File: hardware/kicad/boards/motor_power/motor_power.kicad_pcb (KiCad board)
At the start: 2 copper layers, 104 x 104 mm, 58 parts, among them J1 PWM fra MCU, J2 MCP PWM, J3 DC Motor, J4 3-fase ind, J5 3-fase ud, J6 V1 ud til load, J7 Screw_Terminal_01x03, Q1 IRF540N, Q2 IRF530, SW1 Switch, U1 MCP601, U2 NE555, U3 ILD74, U4 MCP601, U5 IR2110, U6 LM7805, U7 4N25, U8 IR2110

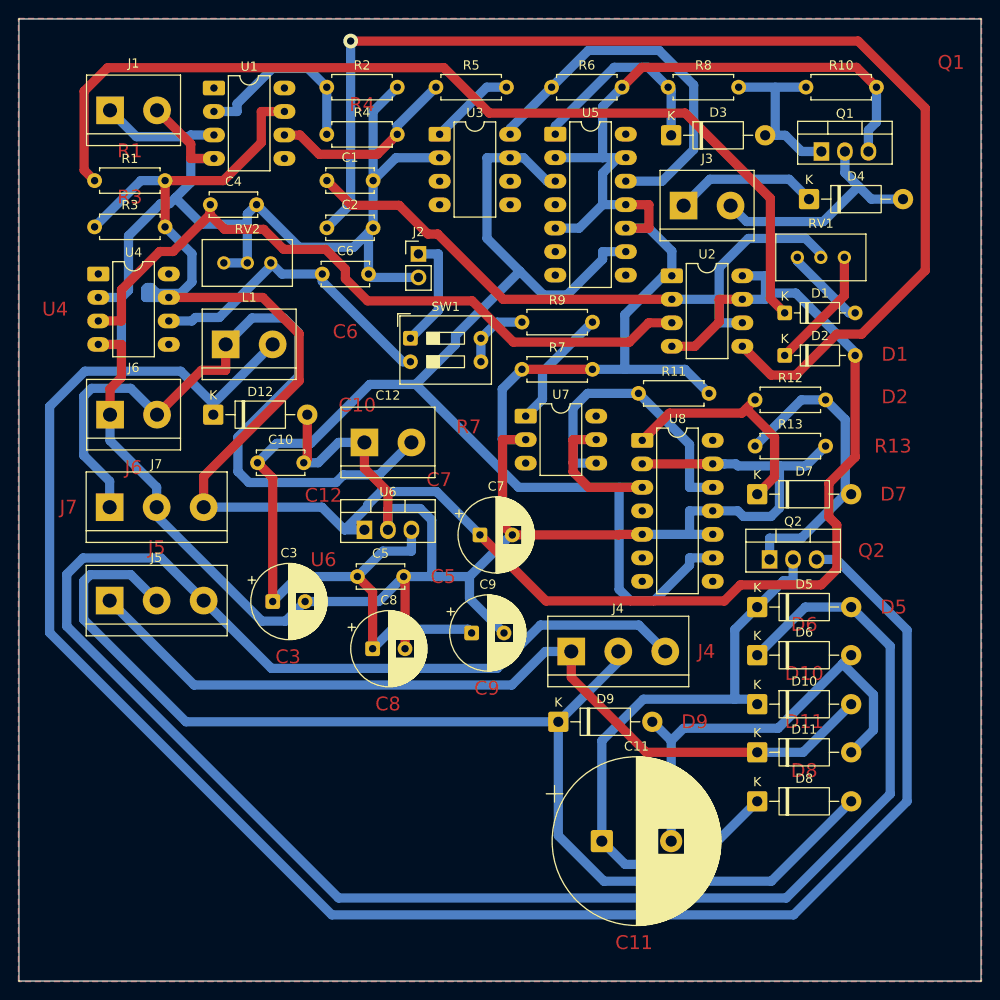
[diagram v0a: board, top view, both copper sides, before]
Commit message: motor_power: re-route with 0 vias (single-sided clean)
Bypass caps placed adjacent to their ICs (C1/C2 by the 555) so the 555-CONT net
no longer needs an inter-layer link. Fully routed: 0 vias, 0 unconnected pads.
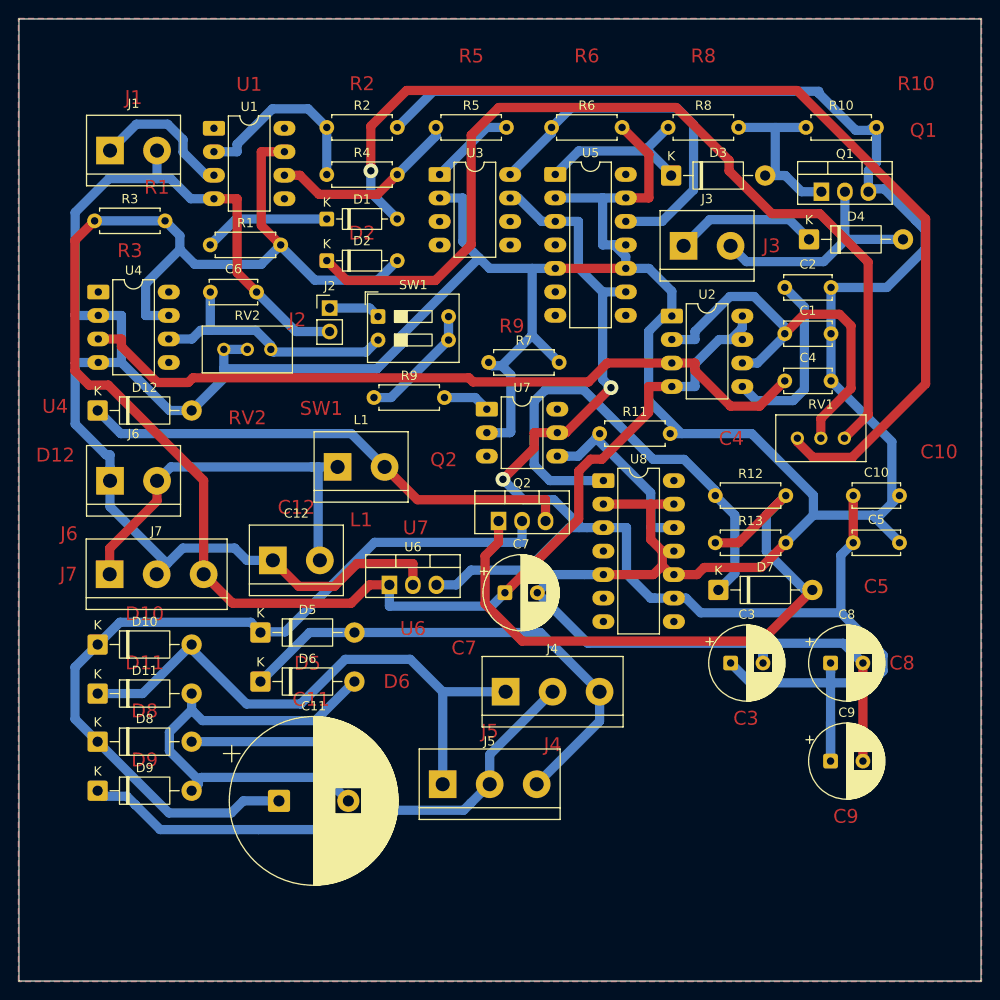
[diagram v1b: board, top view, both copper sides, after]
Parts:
- moved D10 71.6 mm to (28.5, 87.6)
- moved D8 71.6 mm to (28.5, 98.1)
- moved D11 71.6 mm to (28.5, 92.9)
- moved C4 65.0 mm to (102.8, 59.1)
- moved C10 64.5 mm to (110.2, 71.5)
- moved D6 53.8 mm to (46.1, 91.6)
- moved D5 53.8 mm to (46.1, 86.3)
- moved C5 53.7 mm to (110.2, 76.6)
- moved C1 52.2 mm to (102.8, 54.0)
- moved D2 50.6 mm to (53.3, 46.1)
- moved D1 50.5 mm to (53.3, 41.6)
- moved D9 50.4 mm to (28.5, 103.4)
- moved C3 49.9 mm to (96.9, 89.6)
- moved C2 49.9 mm to (102.8, 49.0)
- moved C8 49.5 mm to (107.7, 89.6)
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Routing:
- net Net-(D5-A): track 219.2 -> 54.3 mm
- net /SW: track 197.3 -> 54.7 mm
- net Net-(U2-CONT): track 129.7 -> 19.7 mm, vias 1 -> 0
- net GND: track 434.1 -> 540.6 mm
- net Net-(D1-A): track 8.98 -> 114.6 mm, vias 0 -> 1
- net Net-(D1-K): track 104.2 -> 13.8 mm
- net Net-(D2-K): track 13.3 -> 101.8 mm
- net Net-(D8-A): track 129.2 -> 83.0 mm
- net V1: track 83.3 -> 42.5 mm
- net Net-(D7-A): track 33.9 -> 72.2 mm
- net +15V2: track 197.4 -> 165.9 mm, vias 0 -> 2
- net Net-(D10-A): track 93.8 -> 62.7 mm
- net +5v: track 223.6 -> 193.4 mm
- net Net-(D7-K): track 25.3 -> 52.0 mm
- net Net-(U2-THRES): track 69.6 -> 44.8 mm
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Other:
- board text added: "C4"
- board text added: "D12"
- board text added: "J1"
- board text added: "J2"
- board text added: "J3"
- board text added: "L1"
- board text added: "R10"
- board text added: "R2"
- board text added: "R5"
- board text added: "R6"
- board text added: "R8"
- board text added: "R9"
- board text added: "RV2"
- board text added: "SW1"
- board text added: "U1"
- board text added: "U7"
- board text removed: "C6"
- board text removed: "D1"
- board text removed: "D7"
- board text removed: "R13"
- board text removed: "R4"
- board text removed: "R7"

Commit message: Refdes on silkscreen, never on top copper
Component reference designators now go on F.SilkS (top silkscreen) instead of
being etched as copper text on F.Cu. Footprint default refs are hidden so there's
one clean label per part; placement only avoids pads (silk-over-copper is fine),
so nothing drops. Also fixes the finish step's zone-removal to materialize lists
before Remove() (KiCad-10 SWIG iterators invalidate on mutation). motor_power +
motor_feedback re-finished to silk.
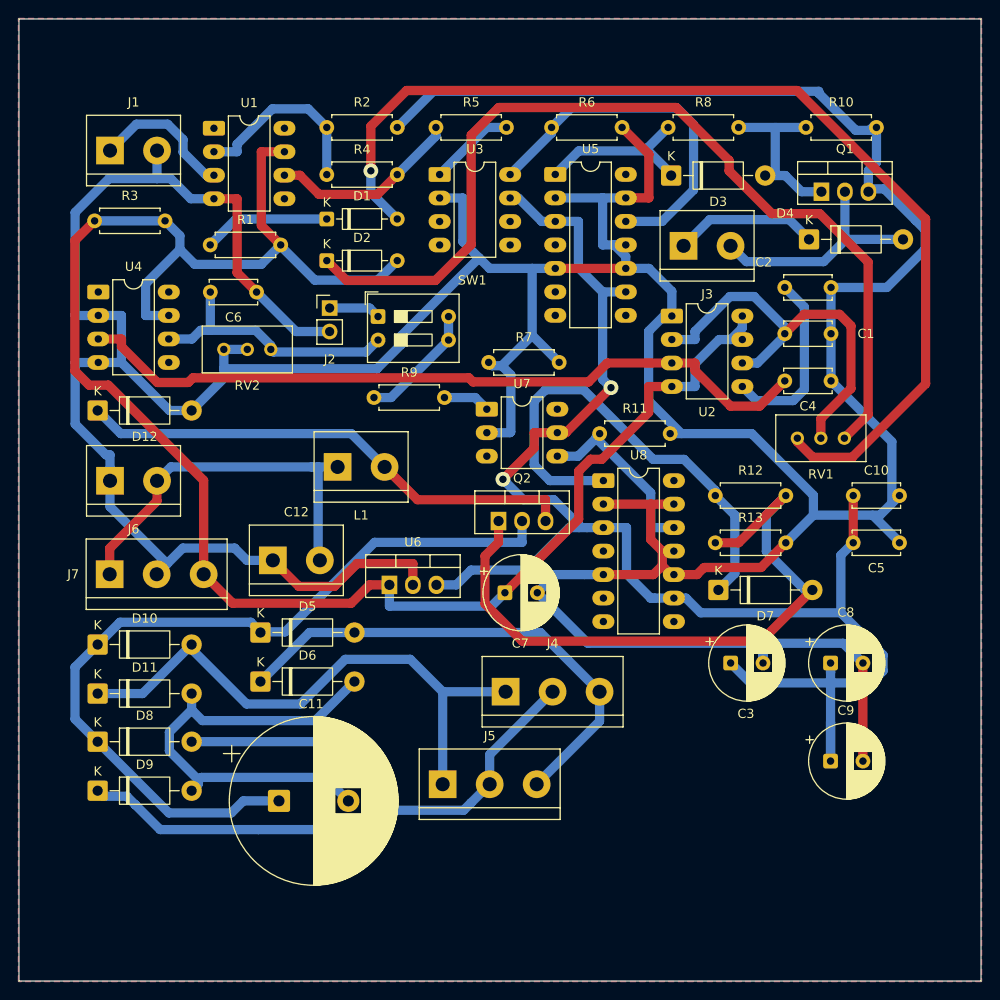
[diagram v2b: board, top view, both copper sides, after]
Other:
- board text added: "C1"
- board text added: "C2"
- board text added: "C6"
- board text added: "D1"
- board text added: "D3"
- board text added: "D4"
- board text added: "D7"
- board text added: "R11"
- board text added: "R12"
- board text added: "R13"
- board text added: "R4"
- board text added: "R7"
- board text added: "RV1"
- board text added: "U2"
- board text added: "U3"
- board text added: "U5"
- board text added: "U8"
